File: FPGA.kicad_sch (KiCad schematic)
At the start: 111 parts, among them U11 IS62WV51216BLL-55TLI, U7 CAT24C128, U8 LFE5U-25F-8MG285C, U9 W25Q128JVP, X1 27MHz

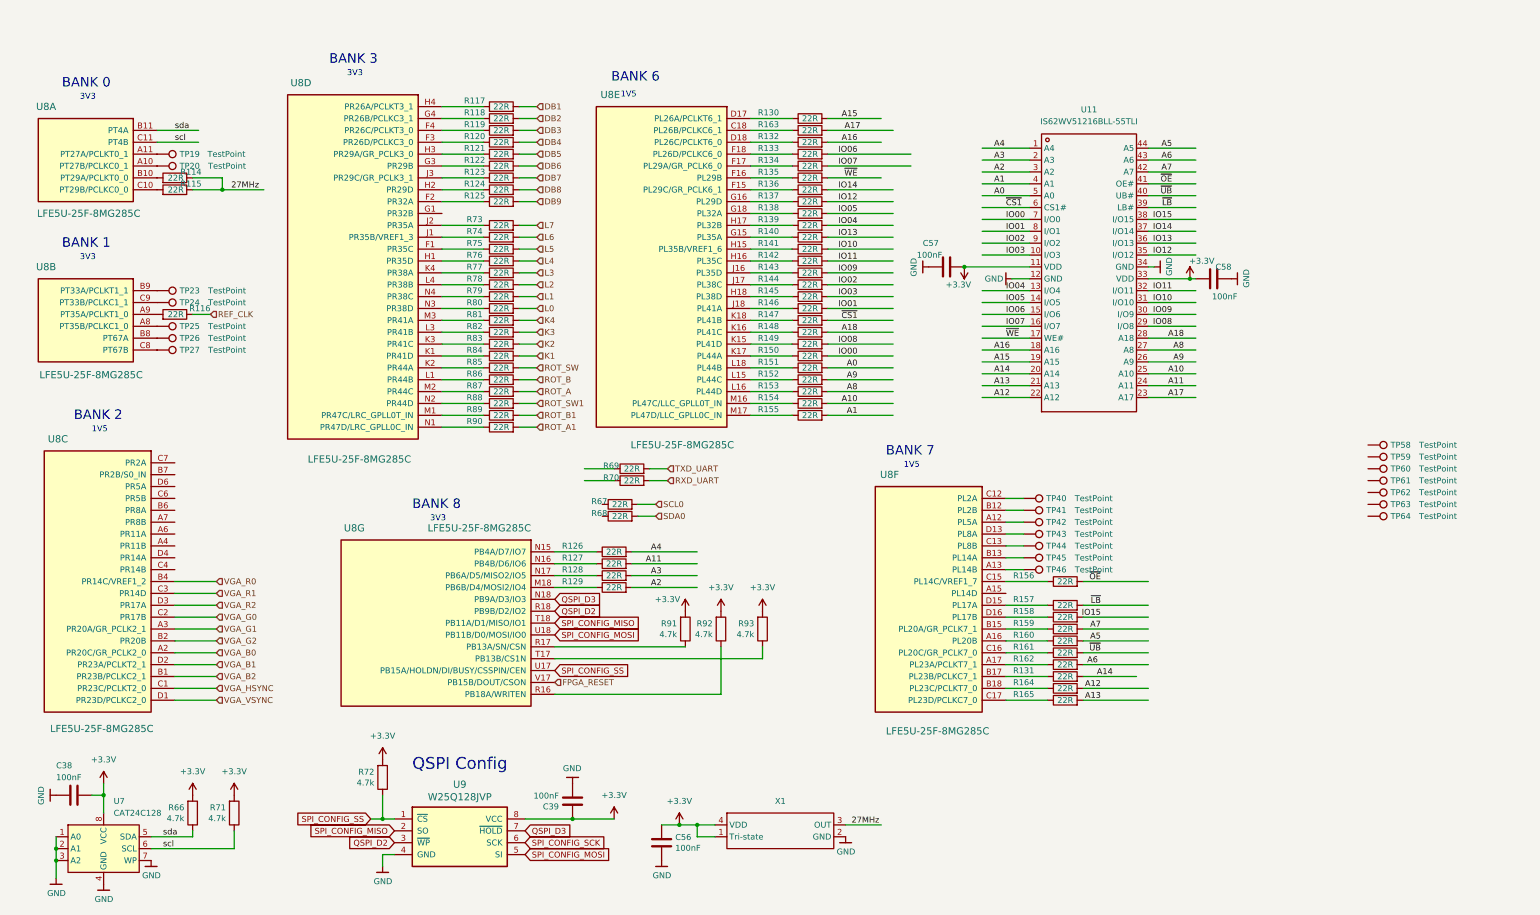
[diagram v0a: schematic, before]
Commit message: Complete SRAM, and routing VGA
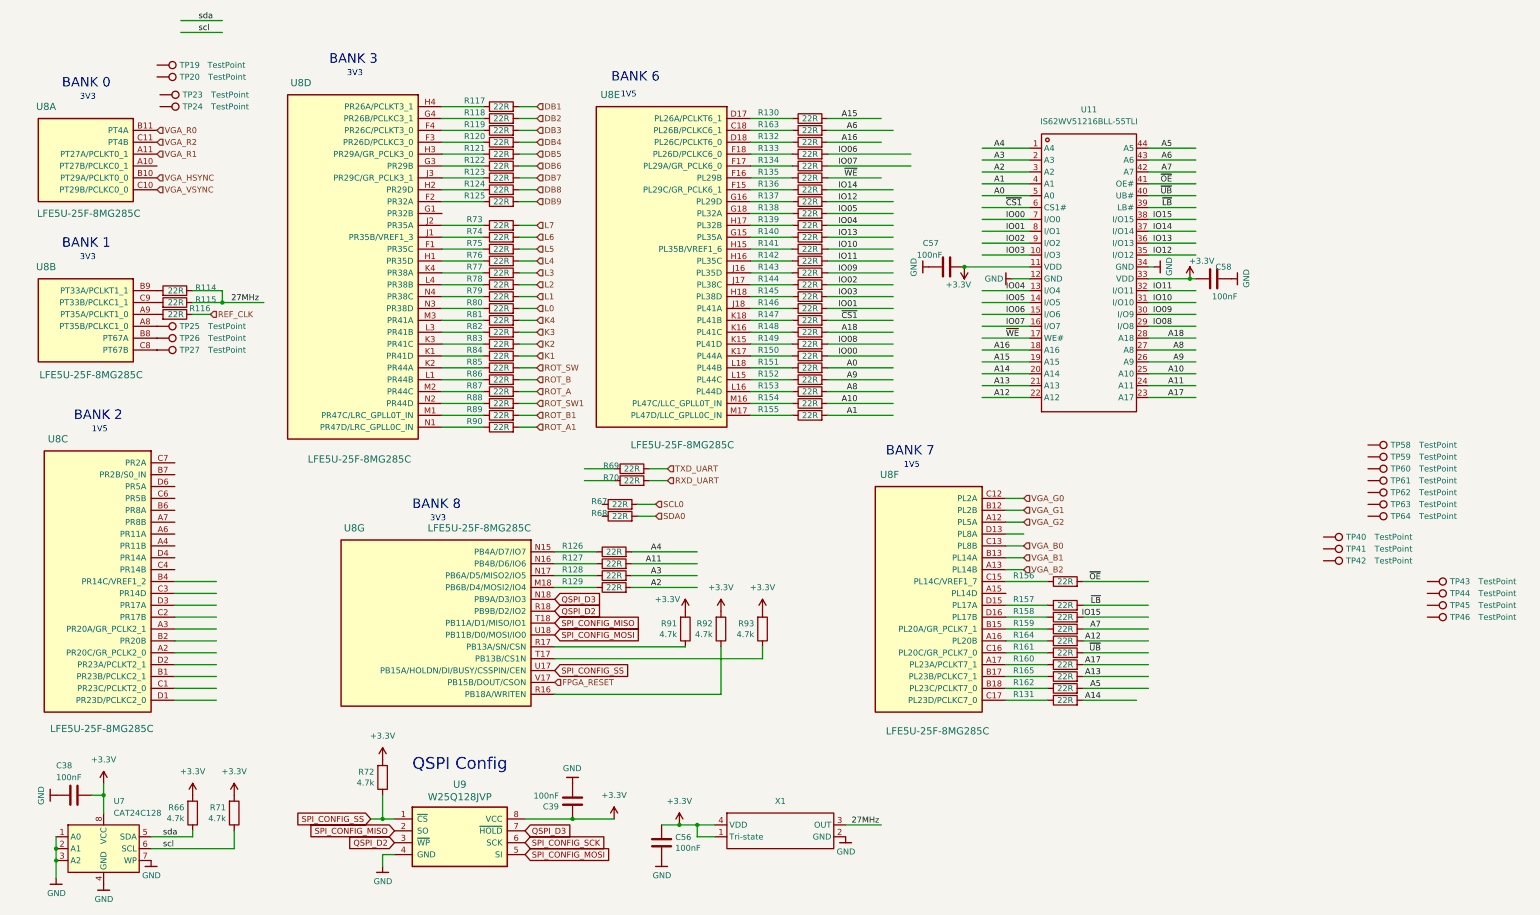
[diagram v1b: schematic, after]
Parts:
- R114, R115, R116, R117, R118, R119, R120, R121, R122, R123, R124, R125, R126, R127, R128, R129, R130, R131, R132, R133, R134, R135, R136, R137, R138, R139, R140, R141, R142, R143, R144, R145, R146, R147, R148, R149, R150, R151, R152, R153, R154, R155, R156, R157, R158, R159, R160, R161, R162, R163, R164, R165, R67, R68, R69, R70, R73, R74, R75, R76, R77, R78, R79, R80, R81, R82, R83, R84, R85, R86, R87, R88, R89, R90: footprint Resistor_SMD:R_01005_0402Metric_Pad0.57x0.30mm_HandSolder -> Resistor_SMD:R_0402_1005Metric_Pad0.72x0.64mm_HandSolder
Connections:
- net A17: now also R160.2; no longer R163.2
- net A5: now also R162.2; no longer R160.2
- net A6: now also R163.2; no longer R162.2
- net VGA_B0: now also U8.C13 (PL8B); no longer U8.A2 (PR20C/GR_PCLK2_0)
- net VGA_B1: now also U8.B13 (PL14A); no longer U8.D2 (PR23A/PCLKT2_1)
- net VGA_B2: now also U8.A13 (PL14B); no longer U8.B1 (PR23B/PCLKC2_1)
- net VGA_G0: now also U8.C12 (PL2A); no longer U8.C2 (PR17B)
- net VGA_G1: now also U8.B12 (PL2B); no longer U8.A3 (PR20A/GR_PCLK2_1)
- net VGA_G2: now also U8.A12 (PL5A); no longer U8.B2 (PR20B)
- net VGA_HSYNC: now also U8.B10 (PT29A/PCLKT0_0); no longer U8.C1 (PR23C/PCLKT2_0)
- net VGA_R0: now also U8.B11 (PT4A); no longer U8.B4 (PR14C/VREF1_2)
- net VGA_R1: now also U8.A11 (PT27A/PCLKT0_1); no longer U8.C3 (PR14D)
- net VGA_R2: now also U8.C11 (PT4B); no longer U8.D3 (PR17A)
- net VGA_VSYNC: now also U8.C10 (PT29B/PCLKC0_0); no longer U8.D1 (PR23D/PCLKC2_0)
- net scl: no longer U8.C11 (PT4B)
- net sda: no longer U8.B11 (PT4A)
- net at U8.A10 (PT27B/PCLKC0_1): no longer TP20.1
- net at TP19.1: no longer U8.A11 (PT27A/PCLKT0_1)
- net at R114.2: now also U8.B9 (PT33A/PCLKT1_1); no longer U8.B10 (PT29A/PCLKT0_0)
- net at R115.2: now also U8.C9 (PT33B/PCLKC1_1); no longer U8.C10 (PT29B/PCLKC0_0)
- net at TP23.1: no longer U8.B9 (PT33A/PCLKT1_1)
- net at TP24.1: no longer U8.C9 (PT33B/PCLKC1_1)
- net at TP42.1: no longer U8.A12 (PL5A)
- net at TP46.1: no longer U8.A13 (PL14B)
- net at U8.A16 (PL20B): now also R164.1; no longer R160.1
- net at U8.A17 (PL23A/PCLKT7_1): now also R160.1; no longer R162.1
- net at TP41.1: no longer U8.B12 (PL2B)
- net at TP45.1: no longer U8.B13 (PL14A)
- net at U8.B17 (PL23B/PCLKC7_1): now also R165.1; no longer R131.1
- net at U8.B18 (PL23C/PCLKT7_0): now also R162.1; no longer R164.1
- net at TP40.1: no longer U8.C12 (PL2A)
- net at TP44.1: no longer U8.C13 (PL8B)
- net at U8.C17 (PL23D/PCLKC7_0): now also R131.1; no longer R165.1
- net at U8.D13 (PL8A): no longer TP43.1
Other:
- moved on the sheet: R114, R115, R131, R160, R162, R164, R165, TP19, TP20, TP23, TP24, TP40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

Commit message: Place db9, encoder, btn and leds. Continue routing.
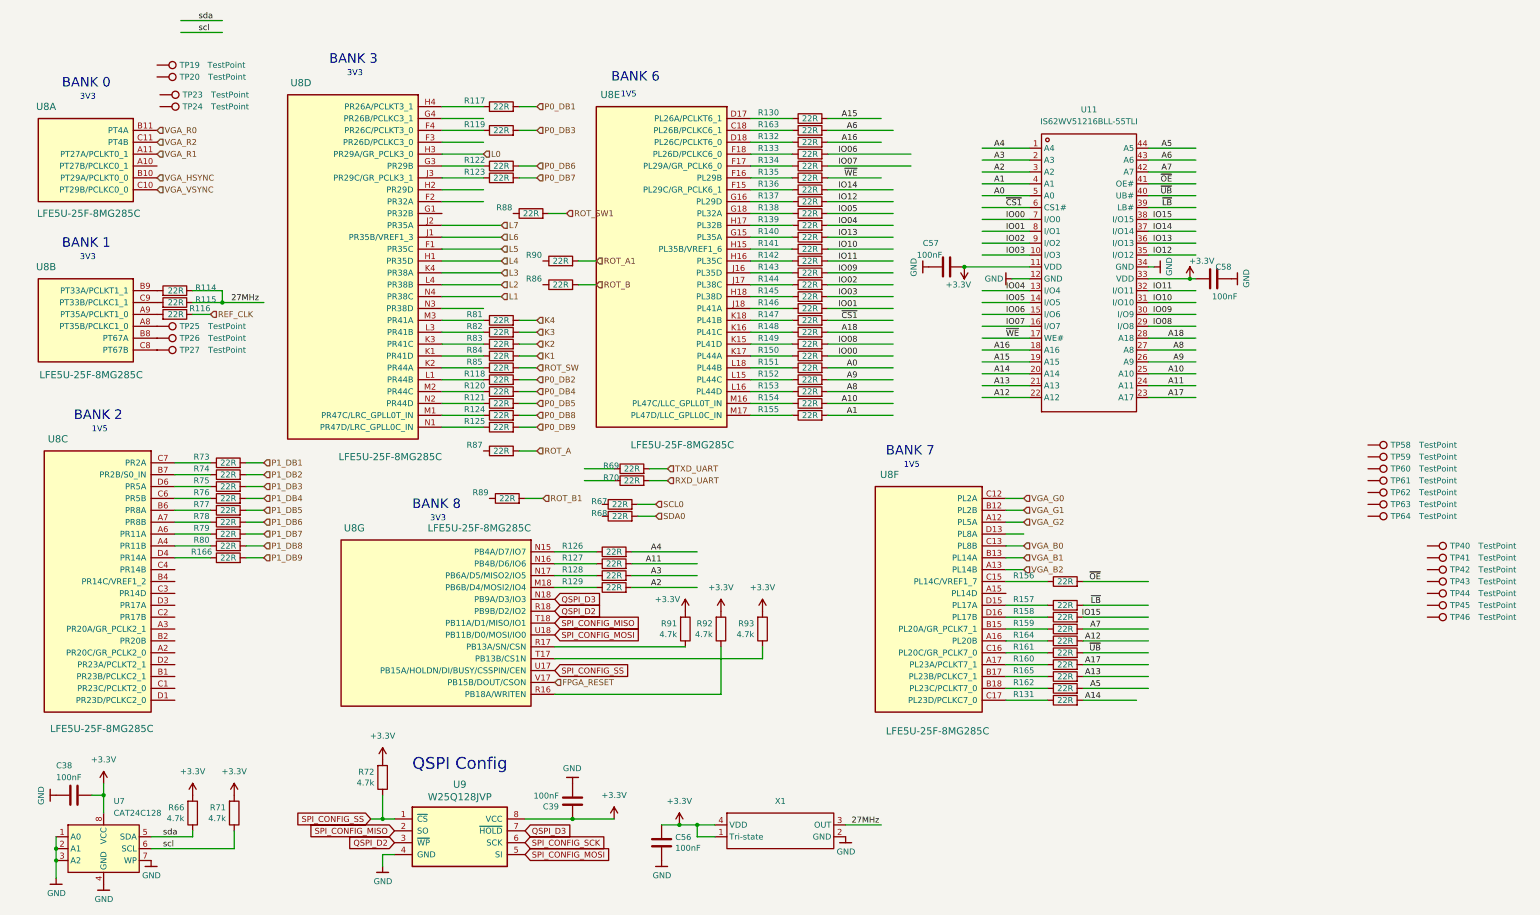
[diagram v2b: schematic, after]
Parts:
- added R166: 22R, Resistor_SMD:R_0402_1005Metric_Pad0.72x0.64mm_HandSolder, symbol Device:R
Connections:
- net L0: now also U8.H3 (PR29A/GR_PCLK3_0); no longer R80.2
- net L1: now also U8.N4 (PR38C); no longer R79.2
- net L2: now also U8.L4 (PR38B); no longer R78.2
- net L3: now also U8.K4 (PR38A); no longer R77.2
- net L4: now also U8.H1 (PR35D); no longer R76.2
- net L5: now also U8.F1 (PR35C); no longer R75.2
- net L6: now also U8.J1 (PR35B/VREF1_3); no longer R74.2
- net L7: now also U8.J2 (PR35A); no longer R73.2
- net at U8.A4 (PR11B): now also R80.1
- net at U8.A6 (PR11A): now also R79.1
- net at U8.A7 (PR8B): now also R78.1
- net at U8.B6 (PR8A): now also R77.1
- net at U8.B7 (PR2B/S0_IN): now also R74.1
- net at U8.C6 (PR5B): now also R76.1
- net at U8.C7 (PR2A): now also R73.1
- net at U8.D4 (PR14A): now also R166.1
- net at U8.D6 (PR5A): now also R75.1
- net at U8.F2 (PR32A): no longer R125.1
- net at U8.F3 (PR26D/PCLKC3_0): no longer R120.1
- net at U8.G4 (PR26B/PCLKC3_1): no longer R118.1
- net at U8.H2 (PR29D): no longer R124.1
- net at R121.1: now also U8.N2 (PR44D); no longer U8.H3 (PR29A/GR_PCLK3_0)
- net at U8.L1 (PR44B): now also R118.1; no longer R86.1
- net at U8.M1 (PR47C/LRC_GPLL0T_IN): now also R124.1; no longer R89.1
- net at U8.M2 (PR44C): now also R120.1; no longer R87.1
- net at U8.N1 (PR47D/LRC_GPLL0C_IN): now also R125.1; no longer R90.1
- net at R88.1: no longer U8.N2 (PR44D)
- net at U8.N3 (PR38D): no longer R80.1
- net DB1 renamed P0_DB1
- net DB2 renamed P0_DB2
- net DB3 renamed P0_DB3
- net DB4 renamed P0_DB4
- net DB5 renamed P0_DB5
- net DB6 renamed P0_DB6
- net DB7 renamed P0_DB7
- net DB8 renamed P0_DB8
- net DB9 renamed P0_DB9
- new net P1_DB1: R73.2
- new net P1_DB2: R74.2
- new net P1_DB3: R75.2
- new net P1_DB4: R76.2
- new net P1_DB5: R77.2
- new net P1_DB6: R78.2
- new net P1_DB7: R79.2
- new net P1_DB8: R80.2
- new net P1_DB9: R166.2
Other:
- moved on the sheet: R118, R120, R121, R124, R125, R86, R87, R88, R89, R90, TP40, TP41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

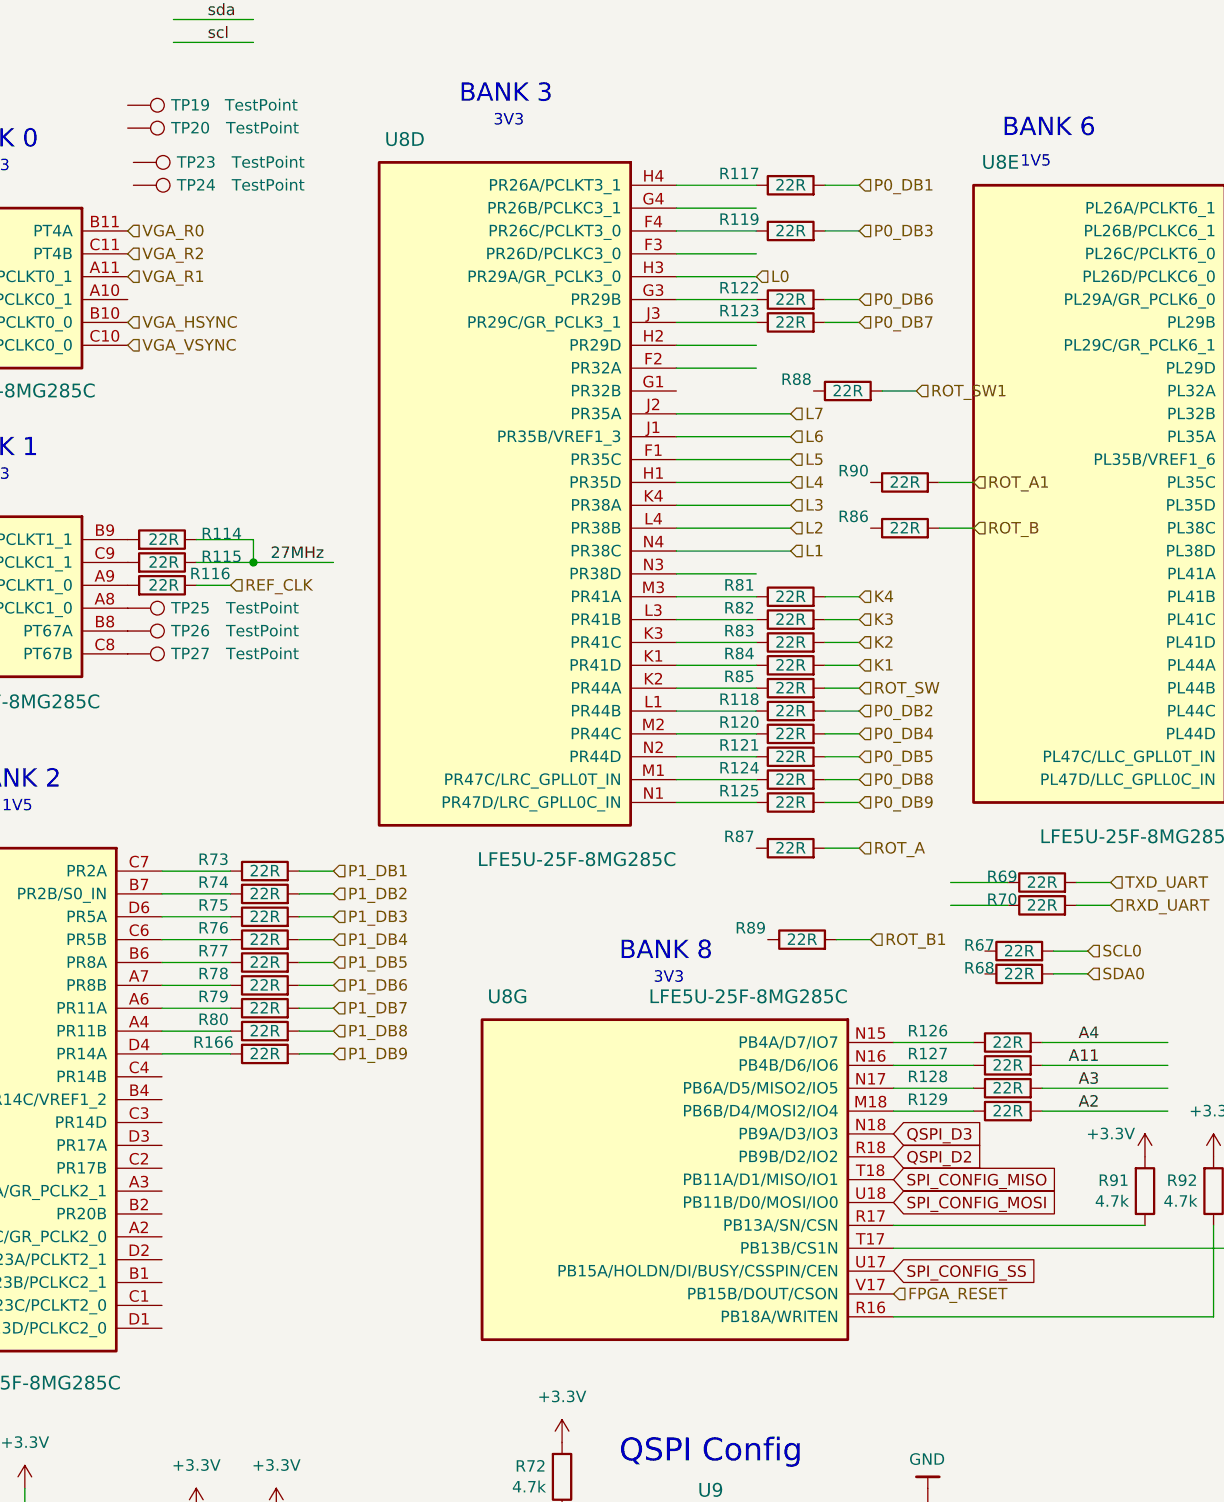
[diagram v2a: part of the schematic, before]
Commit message: Route db9 connectors, rotary, btn and leds.
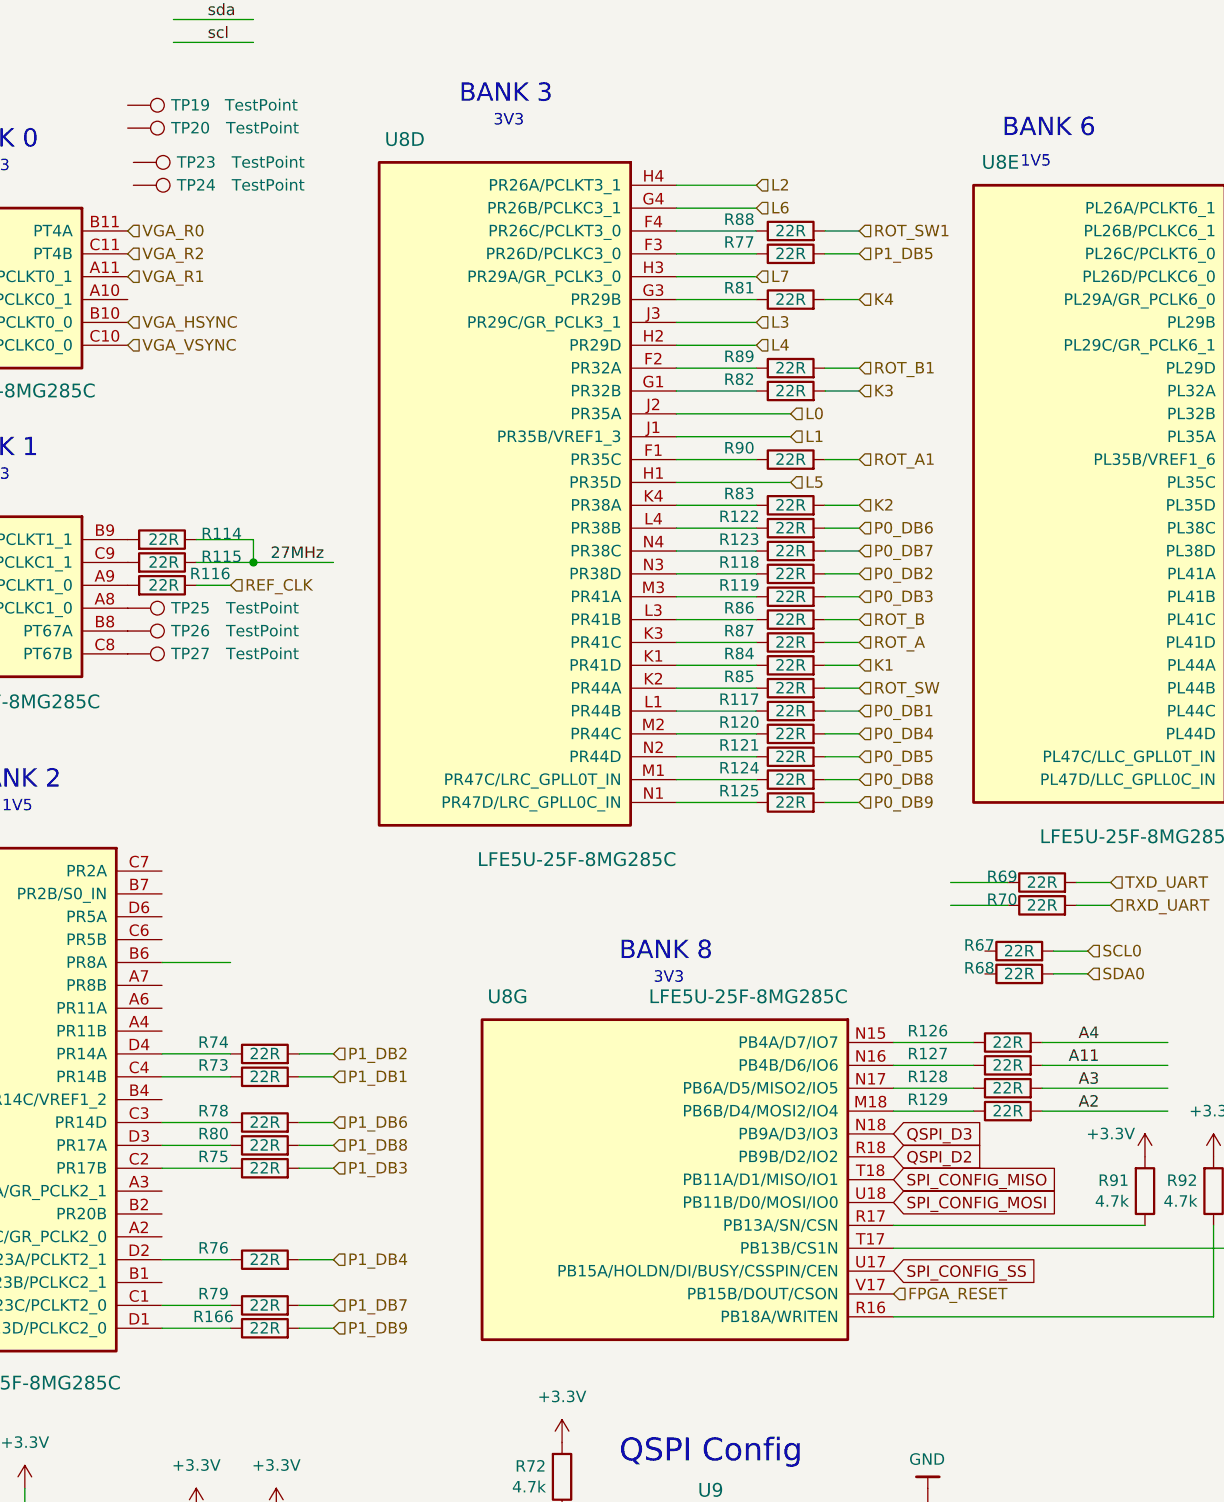
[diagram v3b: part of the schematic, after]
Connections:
- net L0: now also U8.J2 (PR35A); no longer U8.H3 (PR29A/GR_PCLK3_0)
- net L1: now also U8.J1 (PR35B/VREF1_3); no longer U8.N4 (PR38C)
- net L2: now also U8.H4 (PR26A/PCLKT3_1); no longer U8.L4 (PR38B)
- net L3: now also U8.J3 (PR29C/GR_PCLK3_1); no longer U8.K4 (PR38A)
- net L4: now also U8.H2 (PR29D); no longer U8.H1 (PR35D)
- net L5: now also U8.H1 (PR35D); no longer U8.F1 (PR35C)
- net L6: now also U8.G4 (PR26B/PCLKC3_1); no longer U8.J1 (PR35B/VREF1_3)
- net L7: now also U8.H3 (PR29A/GR_PCLK3_0); no longer U8.J2 (PR35A)
- net at U8.A4 (PR11B): no longer R80.1
- net at U8.A6 (PR11A): no longer R79.1
- net at U8.A7 (PR8B): no longer R78.1
- net at U8.B6 (PR8A): no longer R77.1
- net at U8.B7 (PR2B/S0_IN): no longer R74.1
- net at U8.C1 (PR23C/PCLKT2_0): now also R79.1
- net at U8.C2 (PR17B): now also R75.1
- net at U8.C3 (PR14D): now also R78.1
- net at U8.C4 (PR14B): now also R73.1
- net at U8.C6 (PR5B): no longer R76.1
- net at U8.C7 (PR2A): no longer R73.1
- net at U8.D1 (PR23D/PCLKC2_0): now also R166.1
- net at U8.D2 (PR23A/PCLKT2_1): now also R76.1
- net at U8.D3 (PR17A): now also R80.1
- net at U8.D4 (PR14A): now also R74.1; no longer R166.1
- net at U8.D6 (PR5A): no longer R75.1
- net at U8.F2 (PR32A): now also R89.1
- net at U8.F3 (PR26D/PCLKC3_0): now also R77.1
- net at U8.F4 (PR26C/PCLKT3_0): now also R88.1; no longer R119.1
- net at U8.G1 (PR32B): now also R82.1
- net at U8.G3 (PR29B): now also R81.1; no longer R122.1
- net at R117.1: now also U8.L1 (PR44B); no longer U8.H4 (PR26A/PCLKT3_1)
- net at R123.1: now also U8.N4 (PR38C); no longer U8.J3 (PR29C/GR_PCLK3_1)
- net at U8.K3 (PR41C): now also R87.1; no longer R83.1
- net at R118.1: now also U8.N3 (PR38D); no longer U8.L1 (PR44B)
- net at U8.L3 (PR41B): now also R86.1; no longer R82.1
- net at U8.M3 (PR41A): now also R119.1; no longer R81.1
- net at R90.1: now also U8.F1 (PR35C)
- new net: R83.1, U8.K4 (PR38A)
- new net: R122.1, U8.L4 (PR38B)
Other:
- moved on the sheet: R117, R118, R119, R122, R123, R166, R73, R74, R75, R76, R77, R78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
